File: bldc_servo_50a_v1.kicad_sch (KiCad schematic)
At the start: 97 parts, among them IC1 DRV8305NQPHPRQ1, J1 CAN_JST-1, J2 CAN_JST-2, J3 Conn_01x02_Pin, J4 Fan_JST, J5 SWD, M1 Fan_Tacho, Q1 BSC010N04LS, Q2 BSC010N04LS, Q3 BSC010N04LS, Q4 BSC010N04LS, Q5 BSC010N04LS, Q6 BSC010N04LS, SW1 SW_SPDT, U1 LM3480-3.3_Yet to decide, U2 SN65HVD230, U3 LM2596S-5, U4 STM32G431CBT6

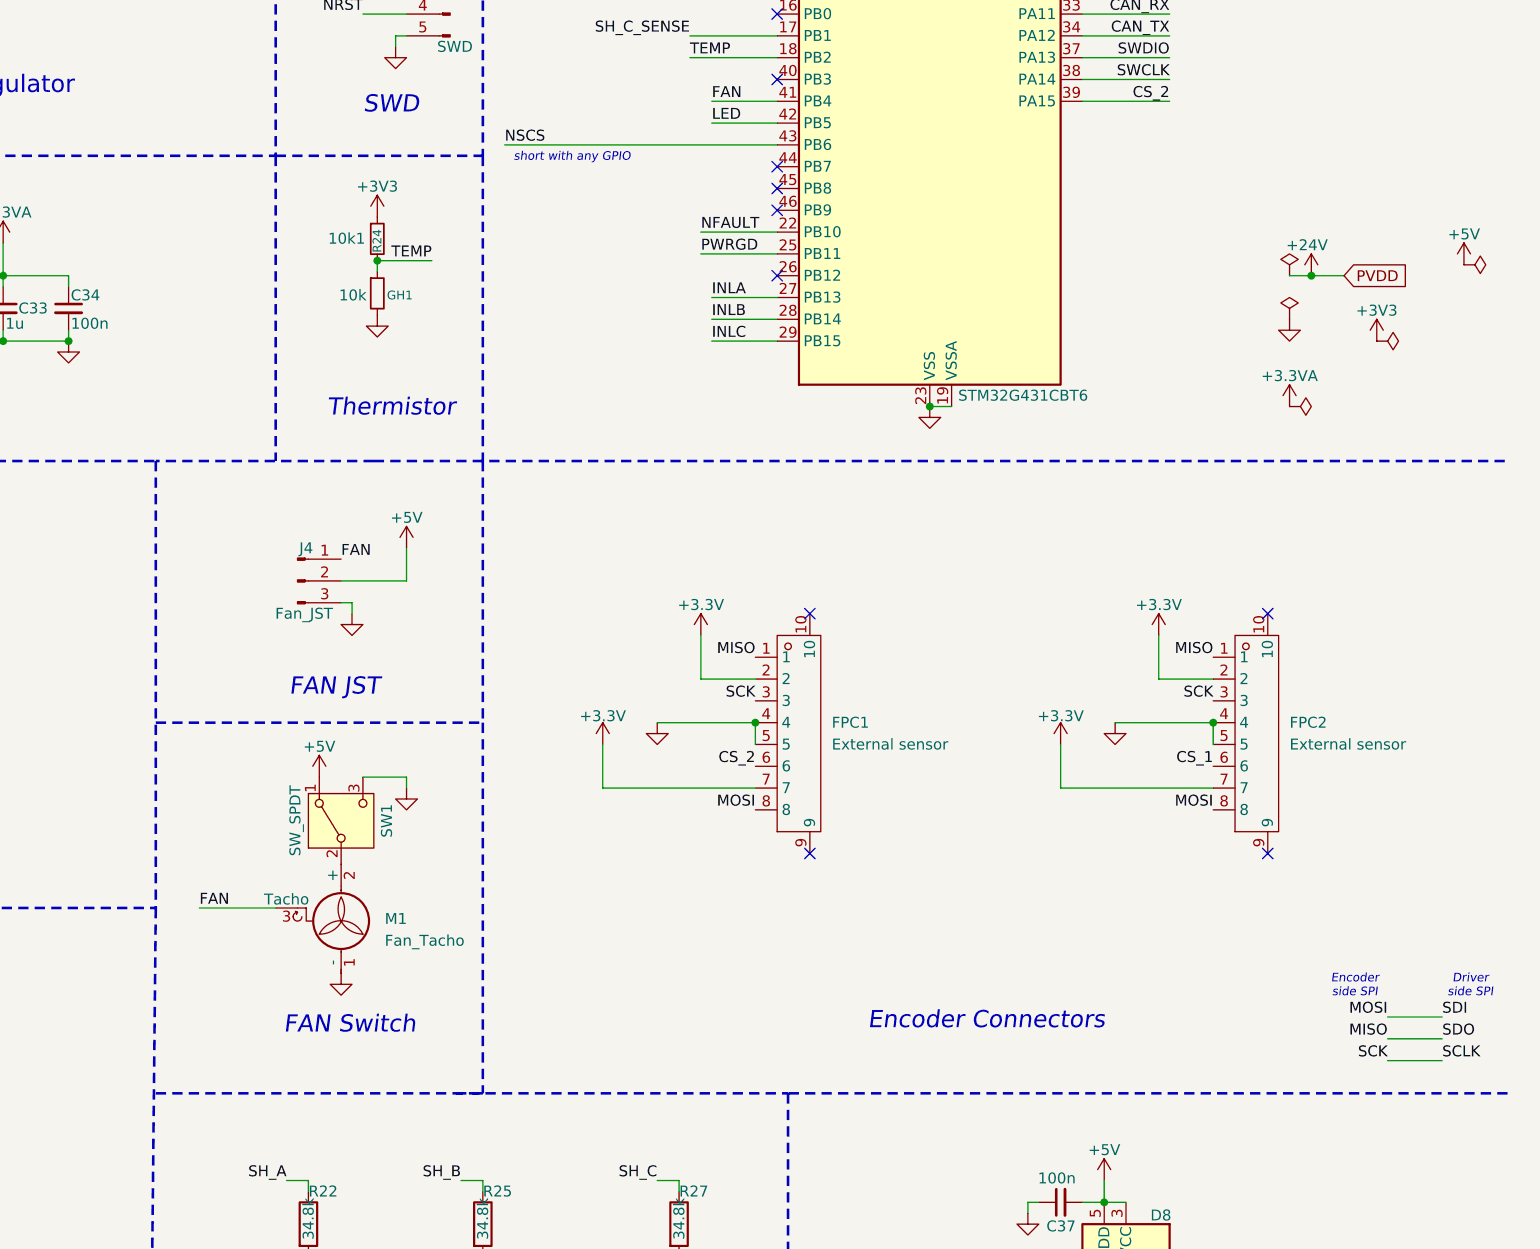
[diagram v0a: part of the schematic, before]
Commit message: Added some nore footprints
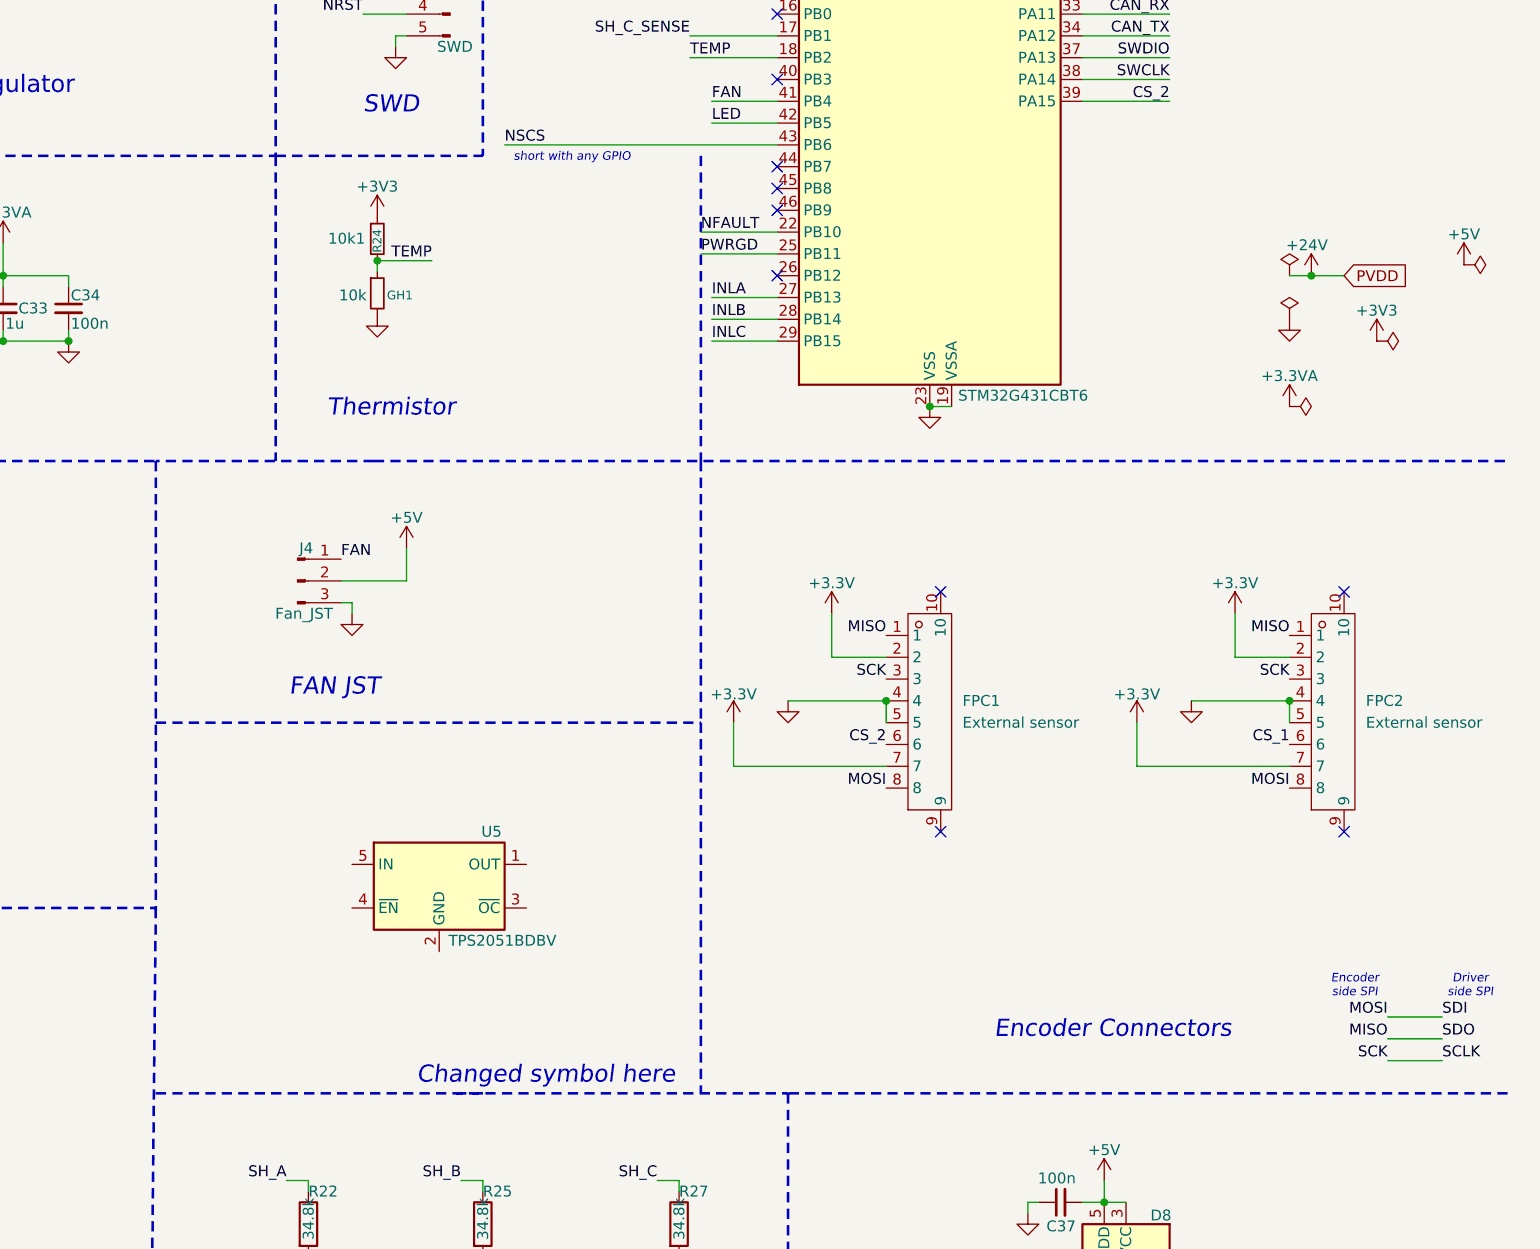
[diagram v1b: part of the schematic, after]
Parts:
- removed M1: Fan_Tacho, symbol Motor:Fan_Tacho
- removed SW1: SW_SPDT, symbol Switch:SW_SPDT
- added U5: TPS2051BDBV, Package_TO_SOT_SMD:SOT-23-5, symbol Power_Management:TPS2051CDBV
- C10, C19, C33: footprint (none) -> Capacitor_SMD:C_0402_1005Metric_Pad0.74x0.62mm_HandSolder
- C26: footprint (none) -> Capacitor_THT:CP_Radial_D13.0mm_P5.00mm; LCSC  (none) -> C599554
- D2: LCSC  (none) -> couldnt find any
- FB1: footprint (none) -> Capacitor_SMD:C_0402_1005Metric_Pad0.74x0.62mm_HandSolder; LCSC  (none) -> hi
- J3: LCSC  (none) -> pads? or connector
- J5: footprint (none) -> Connector_PinHeader_1.00mm:PinHeader_1x05_P1.00mm_Vertical; LCSC  (none) -> berg strips
- R16, R17, R18: footprint (none) -> Resistor_SMD:R_2512_6332Metric_Pad1.40x3.35mm_HandSolder; LCSC  (none) -> C723713
- R23, R26, R28: footprint (none) -> Resistor_SMD:R_0402_1005Metric_Pad0.72x0.64mm_HandSolder; LCSC  (none) -> C477765
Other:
- note added: "Changed symbol here"
- note removed: "FAN Switch"
- moved on the sheet: FPC1, FPC2

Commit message: Changed 5V buck, LDO, shunts
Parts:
- removed D7: 1N5822, Diode_THT:D_DO-201AD_P15.24mm_Horizontal, symbol Diode:1N5822
- removed U1: LM3480-3.3_Yet to decide, Package_TO_SOT_SMD:SOT-23, symbol Regulator_Linear:LM3480-3.3
- removed U3: LM2596S-5, Package_TO_SOT_SMD:TO-263-5_TabPin3, symbol Regulator_Switching:LM2596S-5
- added C38, C39, C40: 10u, symbol Device:C_Small
- added C41: 100n, Capacitor_SMD:C_0402_1005Metric_Pad0.74x0.62mm_HandSolder, symbol Device:C_Small
- added R31, R34, R35: 10, Resistor_SMD:R_0603_1608Metric_Pad0.98x0.95mm_HandSolder, symbol Device:R
- added R32: 100k, symbol Device:R
- added R33: 13.7k, symbol Device:R
- added U3: TLV75533PDBV, Package_TO_SOT_SMD:SOT-23-5, symbol Regulator_Linear:TLV75533PDBV
- added U6: LMR51430, Package_TO_SOT_SMD:SOT-23-6, symbol Regulator_Switching:LMR51430
- C13, C18: value 100n -> 1u; footprint Capacitor_SMD:C_0402_1005Metric_Pad0.74x0.62mm_HandSolder -> (none); LCSC  C77020 -> (none)
- C26: value 680u -> 100n; footprint Capacitor_THT:CP_Radial_D13.0mm_P5.00mm -> Capacitor_SMD:C_0402_1005Metric_Pad0.74x0.62mm_HandSolder; LCSC  C599554 -> (none)
- C35: value 220u -> 10u; footprint Capacitor_SMD:C_0402_1005Metric_Pad0.74x0.62mm_HandSolder -> (none); LCSC  C77020 -> (none)
- L1: value 33uH -> 3.3uH
- R19, R4, R9: footprint Resistor_SMD:R_0402_1005Metric_Pad0.72x0.64mm_HandSolder -> Resistor_SMD:R_2512_6332Metric_Pad1.40x3.35mm_HandSolder; LCSC  C4146794 -> C7370895
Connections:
- net +24V: now also C27.2, C28.2, C29.2, C35.1, U6.3 (VIN), U6.5 (EN)
- net +3.3V: now also U3.5 (OUT)
- net +5V: now also C38.1, C39.1, C40.1, R32.1, U3.1 (IN), U3.3 (EN); no longer C35.2
- net GL_A: now also R31.1; no longer Q2.4 (G)
- net GL_B: now also R34.1; no longer Q4.4 (G)
- net GL_C: now also R35.1; no longer Q6.4 (G)
- net GND: now also C35.2, C38.2, C39.2, C40.2, R33.2, U6.1 (GND); no longer C13.2, C18.2, C27.2, C28.2, C29.2, C35.1
- net 5V_SW: now reaches L1.1
- net 5V_SW: now also C41.1, U6.2 (SW)
- new net: Q4.4 (G), R34.2
- new net: Q2.4 (G), R31.2
- new net: C13.2, C18.2, U3.2 (GND)
- new net: Q6.4 (G), R35.2
- new net 5V_BOOT: C41.2, U6.6 (CB)
- new net 5V_FB: R32.2, R33.1, U6.4 (FB)
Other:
- note added: "LDO (5v->3v3)"
- note removed: "Caps value not finalized"
- note removed: "LDO (5->3v3)"
- moved on the sheet: C13, C18

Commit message: FETs placed
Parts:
- removed R16, R17, R18: 47, Resistor_SMD:R_2512_6332Metric_Pad1.40x3.35mm_HandSolder, symbol Device:R
- added NT1: NetTie_2, symbol Device:NetTie_2
- added R19, R20, R21: 10, Resistor_SMD:R_0603_1608Metric_Pad0.98x0.95mm_HandSolder, symbol Device:R
- C13, L1: footprint (none) -> Capacitor_SMD:C_0402_1005Metric_Pad0.74x0.62mm_HandSolder
- C17: renamed from C18; footprint (none) -> Capacitor_SMD:C_0402_1005Metric_Pad0.74x0.62mm_HandSolder
- C35: renamed from C38; footprint (none) -> Capacitor_SMD:C_0805_2012Metric_Pad1.18x1.45mm_HandSolder
- C36: renamed from C35; footprint (none) -> Capacitor_SMD:C_0805_2012Metric_Pad1.18x1.45mm_HandSolder
- C37: renamed from C39; footprint (none) -> Capacitor_SMD:C_0805_2012Metric_Pad1.18x1.45mm_HandSolder
- C39: renamed from C40; footprint (none) -> Capacitor_SMD:C_0805_2012Metric_Pad1.18x1.45mm_HandSolder
- R23: renamed from R32; footprint (none) -> Resistor_SMD:R_0402_1005Metric_Pad0.72x0.64mm_HandSolder
- R24: renamed from R33; footprint (none) -> Resistor_SMD:R_0402_1005Metric_Pad0.72x0.64mm_HandSolder
- R25: renamed from R20; footprint (none) -> Resistor_SMD:R_0402_1005Metric_Pad0.72x0.64mm_HandSolder
- R27: renamed from R22; footprint (none) -> Resistor_SMD:R_0402_1005Metric_Pad0.72x0.64mm_HandSolder
- R30: renamed from R25; footprint (none) -> Resistor_SMD:R_0402_1005Metric_Pad0.72x0.64mm_HandSolder
- R32: renamed from R27; footprint (none) -> Resistor_SMD:R_0402_1005Metric_Pad0.72x0.64mm_HandSolder
- R6: renamed from R5; footprint (none) -> Resistor_SMD:R_0402_1005Metric_Pad0.72x0.64mm_HandSolder
- renumbered C17 to C18, C27 to C26, C28 to C27, C29 to C28, C30 to C29, C31 to C30, C32 to C31, C33 to C32, C41 to C33, C26 to C38, C36 to C40, C37 to C41, D8 to D7, R34 to R10, R9 to R11, R10 to R12, R11 to R13, R12 to R14, R13 to R15, R14 to R16, R35 to R17, R15 to R18, R31 to R2, R19 to R22, R21 to R26, R23 to R28, R24 to R29, R2 to R3, R26 to R31, R28 to R33, R3 to R4, R4 to R5, R6 to R7, R7 to R8, R8 to R9, U3 to U1, U6 to U3, U5 to U4, U4 to U5
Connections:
- net GND: now also NT1.2; no longer IC1.24 (SP1)
- net PHASE_A: now also R19.1
- net PHASE_B: now also R20.1
- net PHASE_C: now also R21.1
- net R_C_PhaseA: now reaches C26.1
- net R_C_PhaseA: now also R19.2
- net R_C_PhaseC: now reaches C28.1
- net R_C_PhaseC: now also R21.2
- net R_C_PhaseB: now reaches C27.1
- net R_C_PhaseB: now also R20.2
- new net SP1: IC1.24 (SP1), NT1.1

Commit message: Basic tentative component placement for MCU and DRV
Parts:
- added NT1: NetTie_2, symbol Device:NetTie_2
- renumbered NT1 to NT2
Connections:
- net SL_A: now also NT1.2; no longer IC1.23 (SN1)
- new net SN1: IC1.23 (SN1), NT1.1
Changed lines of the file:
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@@
 	)
 	(junction
+		(at 53.34 241.3)
+		(diameter 0)
+		(color 0 0 0 0)
+	)
+	(junction
 		(at 133.35 173.99)
 		(diameter 0)
@@
 	)
 	(junction
-		(at 53.34 241.3)
-		(diameter 0)
-		(color 0 0 0 0)
-	)
-	(junction
 		(at 213.36 220.98)
 		(diameter 0)
@@
 	(wire
 		(pts
-			(xy 78.74 30.48) (xy 78.74 29.21)
+			(xy 26.67 241.3) (xy 41.91 241.3)
 		)
 		(stroke
@@
 	(wire
 		(pts
-			(xy 26.67 241.3) (xy 53.34 241.3)
+			(xy 78.74 30.48) (xy 78.74 29.21)
 		)
 		(stroke
@@
 	(wire
 		(pts
+			(xy 46.99 241.3) (xy 53.34 241.3)
+		)
+		(stroke
+			(width 0)
+			(type default)
+		)
+	)
+	(wire
+		(pts
 			(xy 314.96 91.44) (xy 322.58 91.44)
 		)
@@
 	(wire
 		(pts
+			(xy 53.34 241.3) (xy 53.34 243.84)
+		)
+		(stroke
+			(width 0)
+			(type default)
+		)
+	)
+	(wire
+		(pts
 			(xy 350.52 201.93) (xy 355.6 201.93)
 		)
@@
 	(wire
 		(pts
-			(xy 53.34 241.3) (xy 53.34 243.84)
-		)
-		(stroke
-			(width 0)
-			(type default)
-		)
-	)
-	(wire
-		(pts
 			(xy 53.34 184.15) (xy 53.34 186.69)
 		)
@@
 	)
 	(symbol
+		(lib_id "Device:NetTie_2")
+		(at 44.45 241.3 0)
+		(unit 1)
+		(exclude_from_sim no)
+		(in_bom no)
+		(on_board yes)
+		(dnp no)
+		(property "Reference" "NT1"
+			(at 44.45 242.316 0)
+			(effects
+				(font
+					(size 1.27 1.27)
+				)
+			)
+		)
+		(property "Value" "NetTie_2"
+			(at 43.942 239.776 0)
+			(effects
+				(font
+					(size 1.27 1.27)
+				)
+			)
+		)
+		(property "Footprint" ""
+			(at 44.45 241.3 0)
+			(effects
+				(font
+					(size 1.27 1.27)
+				)
+				(hide yes)
+			)
+		)
+		(property "Datasheet" "~"
+			(at 44.45 241.3 0)
+			(effects
+				(font
+					(size 1.27 1.27)
+				)
+				(hide yes)
+			)
+		)
+		(property "Description" "Net tie, 2 pins"
+			(at 44.45 241.3 0)
+			(effects
+				(font
+					(size 1.27 1.27)
+				)
+				(hide yes)
+			)
+		)
+		(pin "1"
+		)
+		(pin "2"
+		)
+		(instances
+			(project "bldc_servo_50a_v1"
+				(path "/ca0f1187-2401-4955-9ff2-f596d64fa8e9"
+					(reference "NT1")
+					(unit 1)
+				)
+			)
+		)
+	)
+	(symbol
 		(lib_id "Connector:Conn_01x03_Pin")
 		(at 266.7 121.92 0)
@@
 		(dnp no)
 		(fields_autoplaced yes)
-		(property "Reference" "NT1"
+		(property "Reference" "NT2"
 			(at 44.45 247.65 0)
 			(effects
@@
 			(project ""
 				(path "/ca0f1187-2401-4955-9ff2-f596d64fa8e9"
-					(reference "NT1")
+					(reference "NT2")
 					(unit 1)
 				)

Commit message: Removed duplicate V_Sensing
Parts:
- removed C18, C31: 1u, Capacitor_SMD:C_0402_1005Metric_Pad0.74x0.62mm_HandSolder, symbol Device:C_Small
- removed D3, D6: BAT54SW, Package_TO_SOT_SMD:SOT-323_SC-70, symbol Diode:BAT54SW
- removed J3: Conn_01x02_Pin, symbol Connector:Conn_01x02_Pin
- removed R14, R25, R7: 34.8k, Resistor_SMD:R_0402_1005Metric_Pad0.72x0.64mm_HandSolder, symbol Device:R
- removed R15, R26, R8: 5k, Resistor_SMD:R_0402_1005Metric_Pad0.72x0.64mm_HandSolder, symbol Device:R
- added A1: A, Solder_Pads:Solder_Pad_5mmx4mm, symbol Connector:Conn_01x01_Pin
- added B1: B, Solder_Pads:Solder_Pad_5mmx4mm, symbol Connector:Conn_01x01_Pin
- added C30: C, Solder_Pads:Solder_Pad_5mmx4mm, symbol Connector:Conn_01x01_Pin
- added C? (x2): 1u, Capacitor_SMD:C_0402_1005Metric_Pad0.74x0.62mm_HandSolder, symbol Device:C_Small
- added D? (x2): BAT54SW, Package_TO_SOT_SMD:SOT-323_SC-70, symbol Diode:BAT54SW
- added J3: PVDD, Solder_Pads:Solder_Pad_5mmx4mm, symbol Connector:Conn_01x01_Pin
- added J4: GND, Solder_Pads:Solder_Pad_5mmx4mm, symbol Connector:Conn_01x01_Pin
- added NT3: NetTie_2, NetTie:NetTie-2_SMD_Pad0.5mm, symbol Device:NetTie_2
- J1, J2: footprint Connector_JST:JST_PH_B3B-PH-K_1x03_P2.00mm_Vertical -> Connector_JST:JST_EH_B3B-EH-A_1x03_P2.50mm_Vertical
- J6: renamed from J5; footprint Connector_PinHeader_1.00mm:PinHeader_1x05_P1.00mm_Vertical -> Connector_PinHeader_2.54mm:PinHeader_1x05_P2.54mm_Vertical
- NT1, NT2: footprint (none) -> NetTie:NetTie-2_SMD_Pad0.5mm
- renumbered C30 to C31, C32 to C33, C33 to C34, C34 to C35, C35 to C36, C36 to C37, C37 to C38, C38 to C39, C39 to C40, C40 to C41, C41 to C42, J4 to J5
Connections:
- net +24V: now also J3.1 (Pin_1)
- net +3V3: now also D?.2 (K), D?.2 (K)
- net GND: now also NT1.2, C?.2, C?.2, D?.1 (A), D?.1 (A), J4.1 (Pin_1), NT3.2; no longer IC1.20 (SP3), IC1.22 (SP2), R11.2, R22.2, R5.2
- net PHASE_A: now also A1.1 (Pin_1)
- net PHASE_B: now also B1.1 (Pin_1)
- net PHASE_C: now also C30.1 (Pin_1)
- net SL_A: now also IC1.23 (SN1); no longer NT1.2
- net SP1: now also NT1.1, R5.2; no longer NT2.1
- net ASENSE: no longer names the net of C7.1, D1.3 (COM)
- removed net SN1: IC1.23 (SN1), NT1.1
- new net: C?.1, D?.3 (COM) (x2)
- new net SP2: IC1.22 (SP2), NT2.1, R11.2
- new net SP3: IC1.20 (SP3), NT3.1, R22.2
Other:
- moved on the sheet: C42, C7, D1, D7, J5, R27, R28, R30, R31, R32, R33

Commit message: Structure for PCB, tentative
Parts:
- JP1: footprint (none) -> Jumper:SolderJumper-2_P1.3mm_Open_RoundedPad1.0x1.5mm
- gave numbers to parts that had none: 4
- renumbered C11 to C10, C12 to C11, C13 to C12, C14 to C13, C15 to C14, C16 to C15, C17 to C16, C19 to C17, C20 to C18, C21 to C19, C22 to C20, C23 to C21, C24 to C22, C25 to C23, C26 to C24, C27 to C25, C28 to C26, C29 to C27, C30 to C28, C31 to C29, C33 to C30, C34 to C31, C35 to C32, C36 to C33, C37 to C34, C38 to C35, C39 to C36, C40 to C37, C7 to C38, C41 to C39, C8 to C7, C9 to C8, C10 to C9, D2 to D1, D4 to D2, D5 to D3, D1 to D4, J5 to J3, J3 to J4, J4 to J5, R12 to R10, R13 to R11, R16 to R12, R17 to R13, R18 to R14, R19 to R15, R20 to R16, R21 to R17, R22 to R18, R23 to R19, R24 to R20, R27 to R21, R28 to R22, R29 to R23, R30 to R24, R31 to R25, R32 to R26, R33 to R27, R9 to R7, R10 to R8, R11 to R9
